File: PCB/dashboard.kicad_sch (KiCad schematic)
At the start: 0 parts

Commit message: [Schem] Finished the Hierarchy Labels of all the pages
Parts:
- added U16: TFT_320x240, Display-extra:TFT-320x240, symbol tft_320x240:TFT_320x240
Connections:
- new net +3.3V: U16.1 (VCC)
- new net Dash_CLK: U16.10 (T_CLK), U16.18 (SD_SCK), U16.7 (SCK)
- new net Dash_MISO: U16.13 (T_DO), U16.17 (SD_MISO), U16.9 (MISO)
- new net Dash_MOSI: U16.12 (T_DIN), U16.16 (SD_MOSI), U16.6 (MOSI)
- new net GND: U16.2 (GND)
- new net SD_CS: U16.15 (SD_CS)
- new net TFT_BL: U16.8 (LED)
- new net TFT_CS: U16.3 (CS)
- new net TFT_DC: U16.5 (DC)
- new net TFT_RST: U16.4 (RST)
- new net T_CS: U16.11 (T_CS)
- new net T_IRQ: U16.14 (T_IRQ)
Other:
- note added: "Future Work: More Dashboard Things. (Currently,Only the screen & Main Power Switch)"

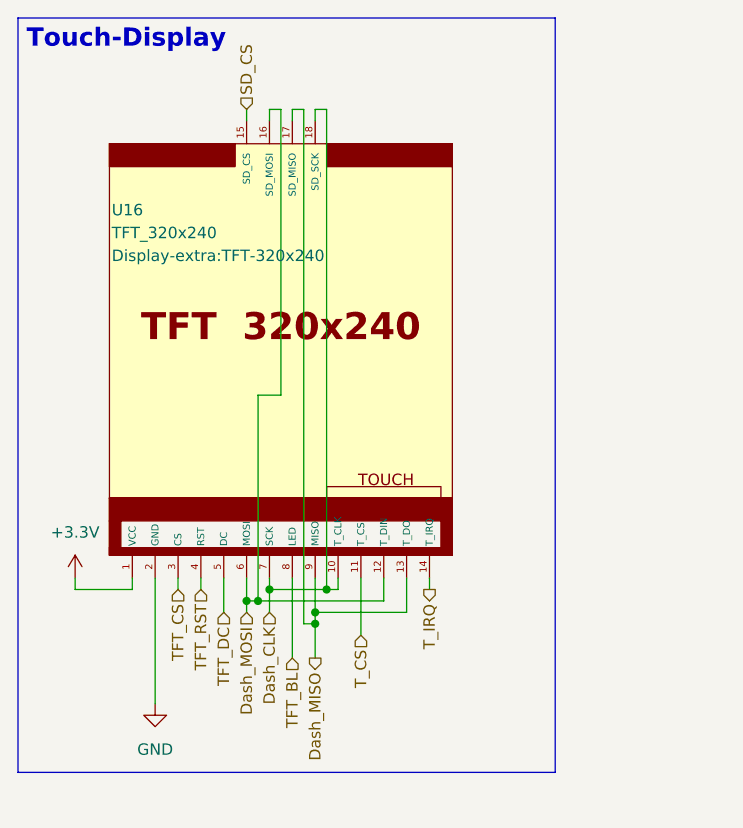
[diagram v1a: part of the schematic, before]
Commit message: [Schem] Added all the net labels and connected the Dashboard screen
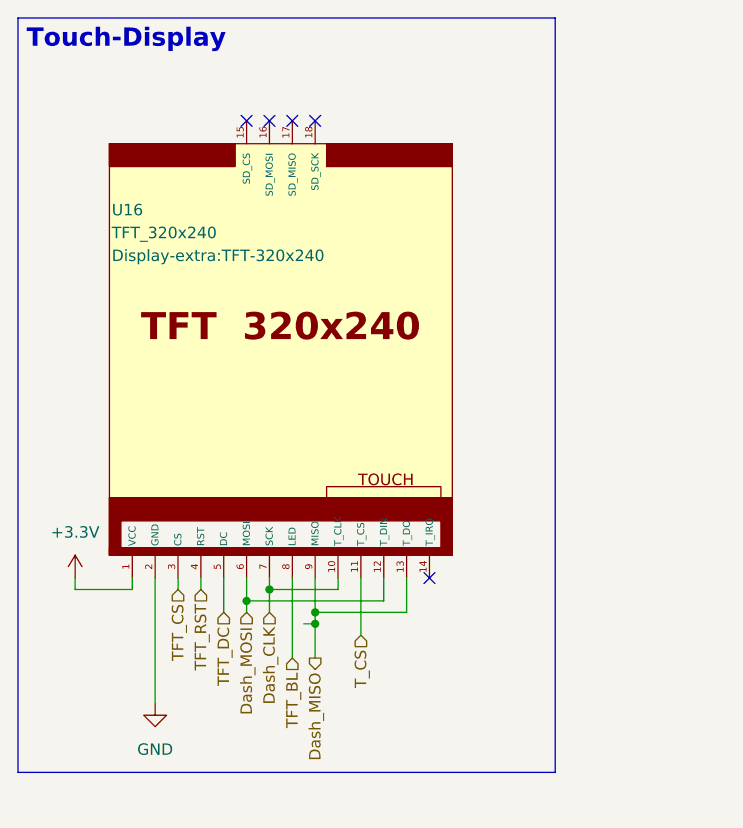
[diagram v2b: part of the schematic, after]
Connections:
- net Dash_CLK: no longer U16.18 (SD_SCK)
- net Dash_MISO: no longer U16.17 (SD_MISO)
- net Dash_MOSI: no longer U16.16 (SD_MOSI)
- net SD_CS: no longer names the net of U16.15 (SD_CS)
- net T_IRQ: no longer names the net of U16.14 (T_IRQ)
- no-connect marks 0 -> 5
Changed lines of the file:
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@@
-	)
-	(junction
-		(at 48.26 77.47)
-		(diameter 0)
-		(color 0 0 0 0)
 	)
 	(junction
@@
 	)
 	(junction
-		(at 40.64 78.74)
-		(diameter 0)
-		(color 0 0 0 0)
-	)
-	(junction
 		(at 46.99 80.01)
 		(diameter 0)
 		(color 0 0 0 0)
 	)
-	(wire
-		(pts
-			(xy 59.69 77.47) (xy 59.69 76.2)
-		)
-		(stroke
-			(width 0)
-			(type default)
-		)
+	(no_connect
+		(at 59.69 76.2)
+	)
+	(no_connect
+		(at 46.99 25.4)
+	)
+	(no_connect
+		(at 41.91 25.4)
+	)
+	(no_connect
+		(at 44.45 25.4)
+	)
+	(no_connect
+		(at 39.37 25.4)
 	)
 	(wire
@@
 	(wire
 		(pts
-			(xy 48.26 24.13) (xy 48.26 77.47)
-		)
-		(stroke
-			(width 0)
-			(type default)
-		)
-	)
-	(wire
-		(pts
-			(xy 46.99 24.13) (xy 48.26 24.13)
-		)
-		(stroke
-			(width 0)
-			(type default)
-		)
-	)
-	(wire
-		(pts
 			(xy 52.07 82.55) (xy 52.07 76.2)
 		)
@@
 	(wire
 		(pts
-			(xy 46.99 24.13) (xy 46.99 25.4)
-		)
-		(stroke
-			(width 0)
-			(type default)
-		)
-	)
-	(wire
-		(pts
 			(xy 46.99 80.01) (xy 46.99 81.28)
 		)
@@
 	(wire
 		(pts
-			(xy 48.26 77.47) (xy 49.53 77.47)
-		)
-		(stroke
-			(width 0)
-			(type default)
-		)
-	)
-	(wire
-		(pts
-			(xy 44.45 24.13) (xy 44.45 25.4)
-		)
-		(stroke
-			(width 0)
-			(type default)
-		)
-	)
-	(wire
-		(pts
 			(xy 45.72 81.28) (xy 46.99 81.28)
 		)
@@
 	(wire
 		(pts
-			(xy 39.37 78.74) (xy 40.64 78.74)
-		)
-		(stroke
-			(width 0)
-			(type default)
-		)
-	)
-	(wire
-		(pts
 			(xy 46.99 76.2) (xy 46.99 80.01)
 		)
@@
 	(wire
 		(pts
-			(xy 45.72 24.13) (xy 45.72 81.28)
-		)
-		(stroke
-			(width 0)
-			(type default)
-		)
-	)
-	(wire
-		(pts
 			(xy 29.21 76.2) (xy 29.21 90.17)
 		)
@@
 	(wire
 		(pts
-			(xy 43.18 24.13) (xy 43.18 55.88)
-		)
-		(stroke
-			(width 0)
-			(type default)
-		)
-	)
-	(wire
-		(pts
 			(xy 41.91 80.01) (xy 41.91 77.47)
 		)
@@
 	(wire
 		(pts
-			(xy 40.64 78.74) (xy 54.61 78.74)
+			(xy 39.37 78.74) (xy 54.61 78.74)
 		)
 		(stroke
@@
 	(wire
 		(pts
-			(xy 41.91 77.47) (xy 48.26 77.47)
+			(xy 41.91 77.47) (xy 49.53 77.47)
 		)
 		(stroke
@@
 	(wire
 		(pts
-			(xy 39.37 24.13) (xy 39.37 25.4)
-		)
-		(stroke
-			(width 0)
-			(type default)
-		)
-	)
-	(wire
-		(pts
-			(xy 41.91 24.13) (xy 41.91 25.4)
-		)
-		(stroke
-			(width 0)
-			(type default)
-		)
-	)
-	(wire
-		(pts
 			(xy 44.45 76.2) (xy 44.45 85.09)
 		)
@@
 	(wire
 		(pts
-			(xy 41.91 24.13) (xy 43.18 24.13)
-		)
-		(stroke
-			(width 0)
-			(type default)
-		)
-	)
-	(wire
-		(pts
 			(xy 20.32 77.47) (xy 26.67 77.47)
 		)
@@
 	(wire
 		(pts
-			(xy 40.64 55.88) (xy 40.64 78.74)
-		)
-		(stroke
-			(width 0)
-			(type default)
-		)
-	)
-	(wire
-		(pts
 			(xy 39.37 78.74) (xy 39.37 80.01)
 		)
@@
 	(wire
 		(pts
-			(xy 40.64 55.88) (xy 43.18 55.88)
-		)
-		(stroke
-			(width 0)
-			(type default)
-		)
-	)
-	(wire
-		(pts
 			(xy 26.67 76.2) (xy 26.67 77.47)
-		)
-		(stroke
-			(width 0)
-			(type default)
-		)
-	)
-	(wire
-		(pts
-			(xy 44.45 24.13) (xy 45.72 24.13)
 		)
 		(stroke
@@
 		)
 	)
-	(hierarchical_label "T_IRQ"
-		(shape output)
-		(at 59.69 77.47 270)
-		(effects
-			(font
-				(size 1.27 1.27)
-			)
-			(justify right)
-		)
-	)
 	(hierarchical_label "Dash_MISO"
 		(shape output)
@@
 		)
 	)
-	(hierarchical_label "SD_CS"
-		(shape input)
-		(at 39.37 24.13 90)
-		(effects
-			(font
-				(size 1.27 1.27)
-			)
-			(justify left)
-		)
-	)

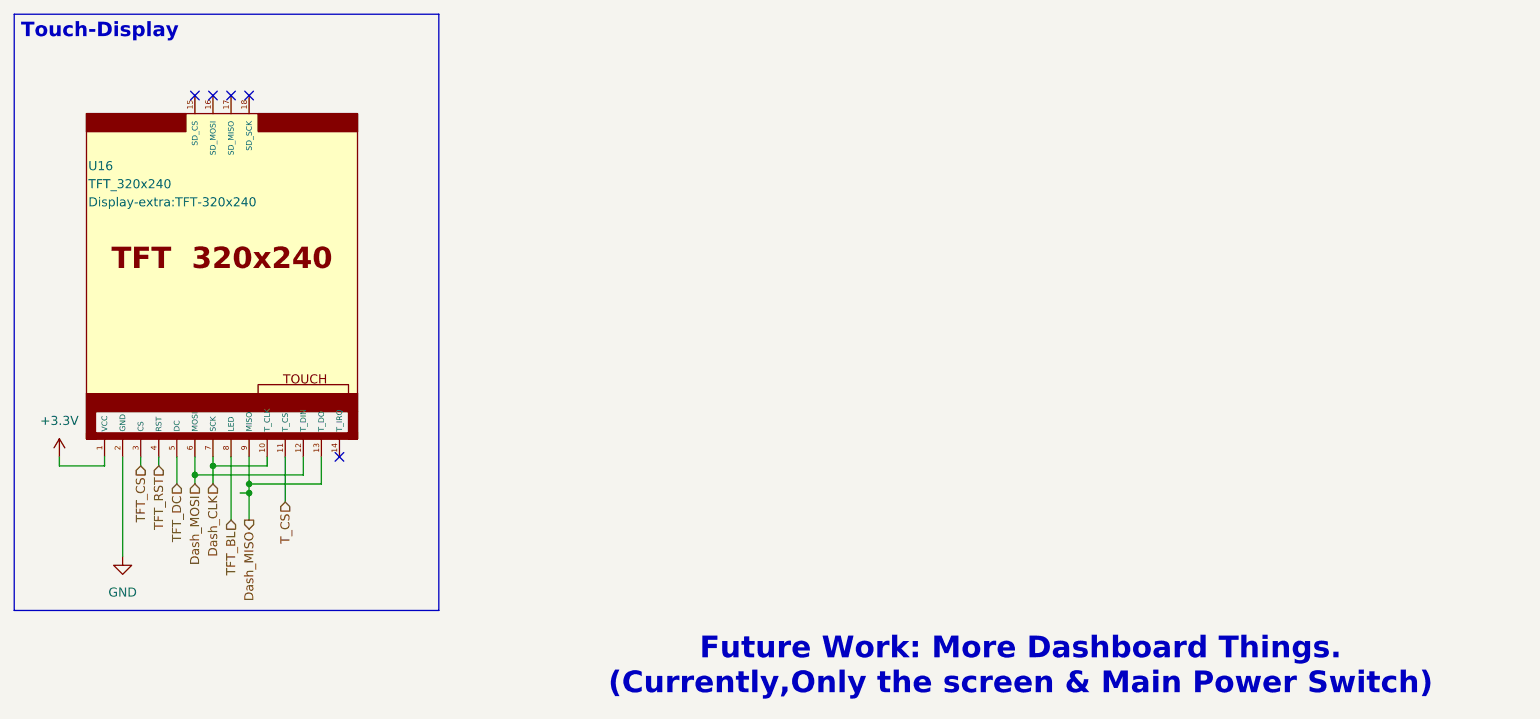
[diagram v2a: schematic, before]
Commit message: [PCB] Splited the PCB into two boards
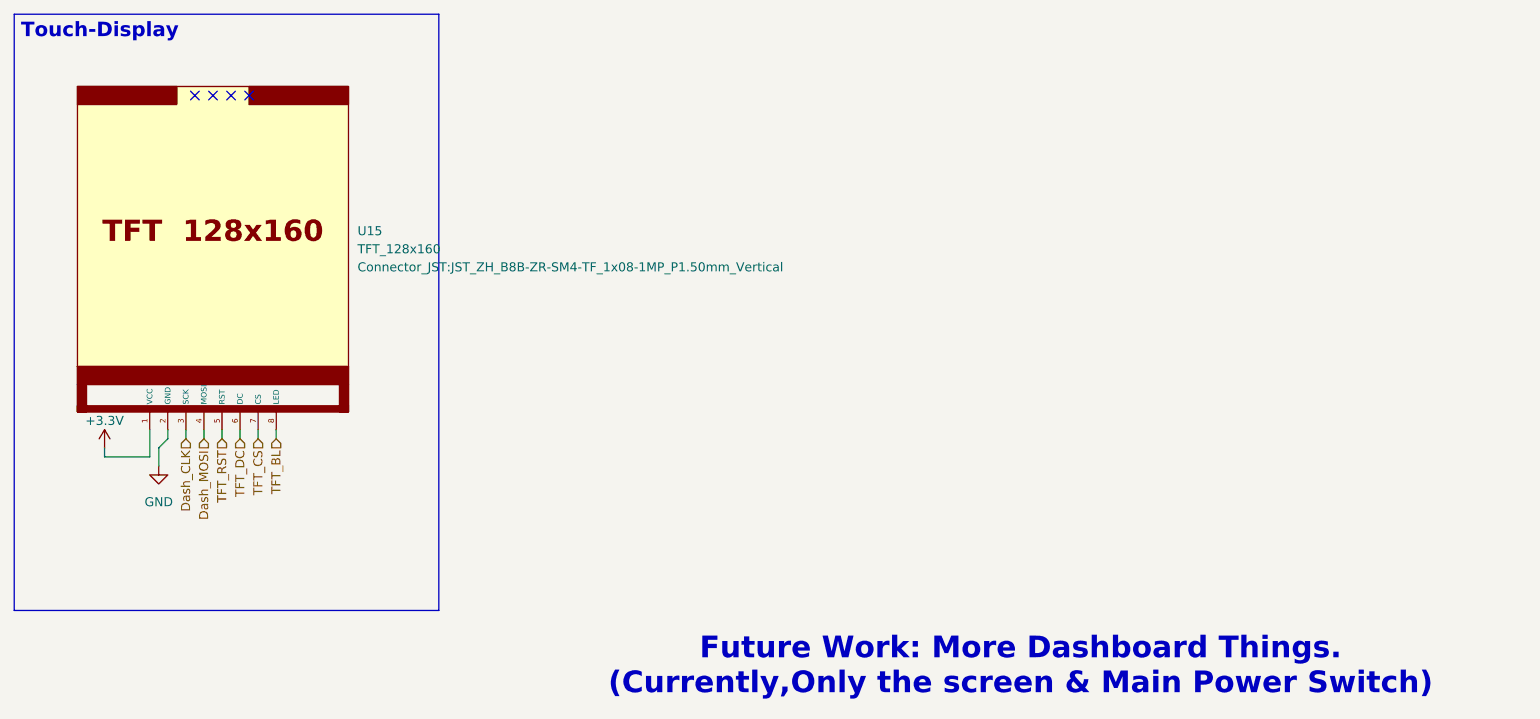
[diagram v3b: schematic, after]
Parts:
- removed U16: TFT_320x240, Display-extra:TFT-320x240, symbol tft_320x240:TFT_320x240
- added U15: TFT_128x160, Connector_JST:JST_ZH_B8B-ZR-SM4-TF_1x08-1MP_P1.50mm_Vertical, symbol tft_320x240:TFT_128*160
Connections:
- net +3.3V: now also U15.1 (VCC)
- net Dash_CLK: now also U15.3 (SCK)
- net Dash_MOSI: now also U15.4 (MOSI)
- net GND: now also U15.2 (GND)
- net TFT_BL: now also U15.8 (LED)
- net TFT_CS: now also U15.7 (CS)
- net TFT_DC: now also U15.6 (DC)
- net TFT_RST: now also U15.5 (RST)
- no-connect marks 5 -> 4
